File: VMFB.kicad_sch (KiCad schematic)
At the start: 112 parts, among them J1 Barrel_Jack_Switch, J10 Conn_01x03_Pin, J11 Conn_01x06_Pin, J12 Conn_01x04_Pin, J13 Conn_01x04_Pin, J14 Conn_01x04_Pin, J2 USB_B, J3 Screw_Terminal_01x02, J4 Screw_Terminal_01x03, J5 Conn_01x03_Pin, J6 Conn_01x04_Pin, J7 Conn_01x04_Pin, J8 Conn_01x04_Pin, J9 Conn_01x02_Pin, Q1 BC547, Q2 BC547, Q3 BC547, Q4 BD139, Q5 TIP41C, Q6 BC547, U1 LM358, U2 NE555P, U3 NE555P, U4 NE555P, U5 NE555P

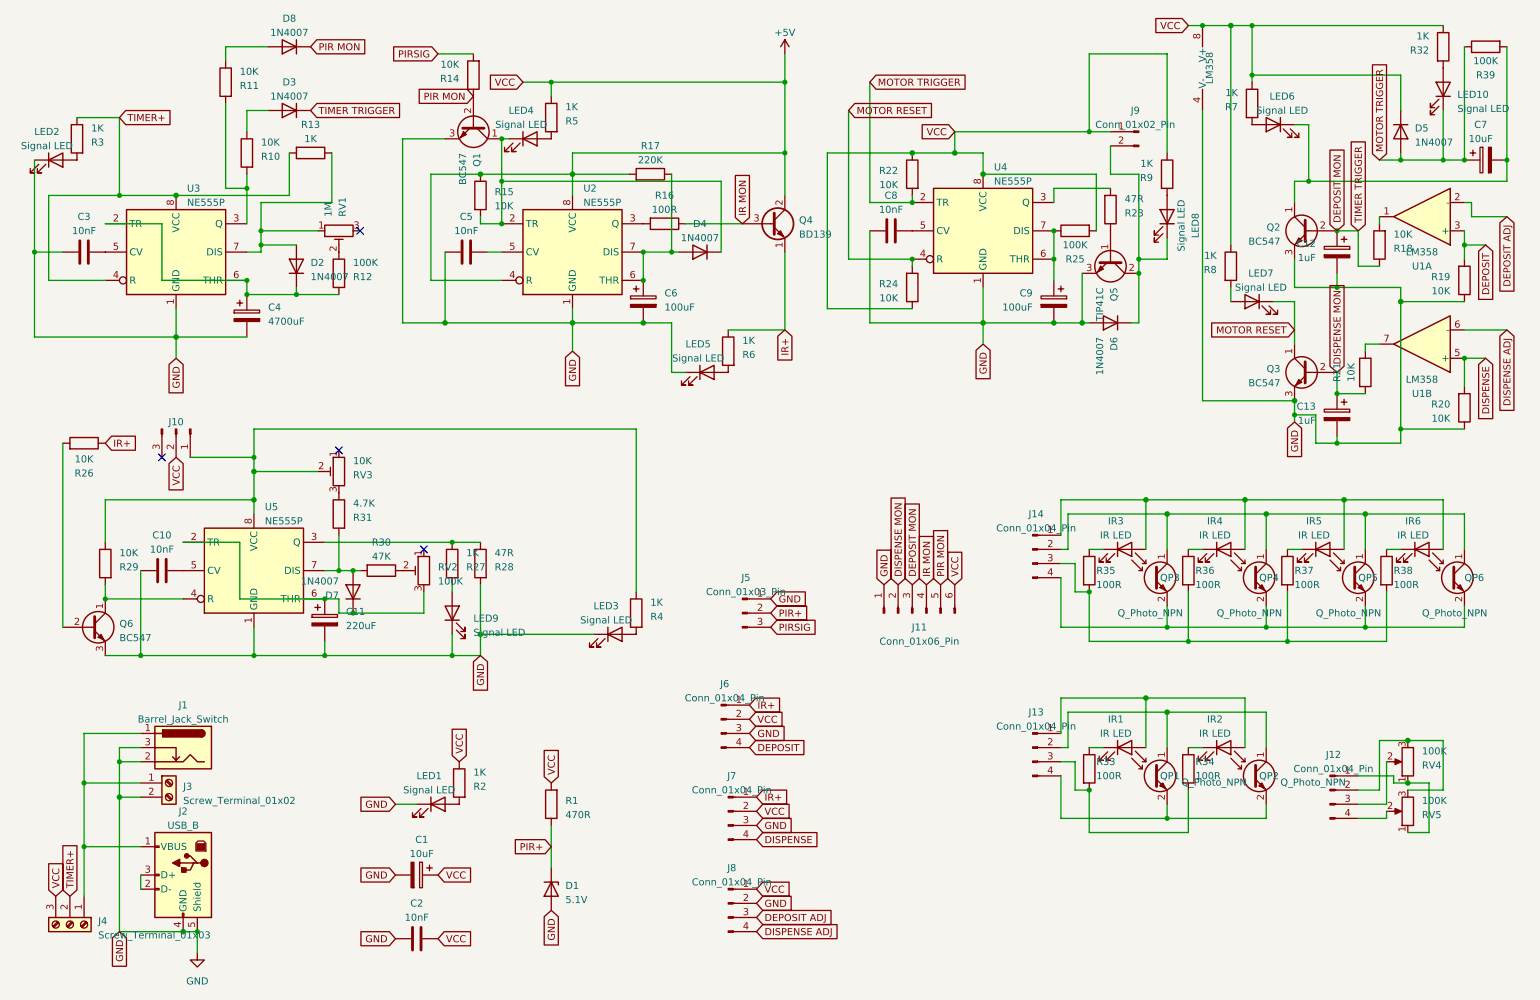
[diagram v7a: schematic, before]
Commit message: changed signal LED resistors to 10K from 1K.
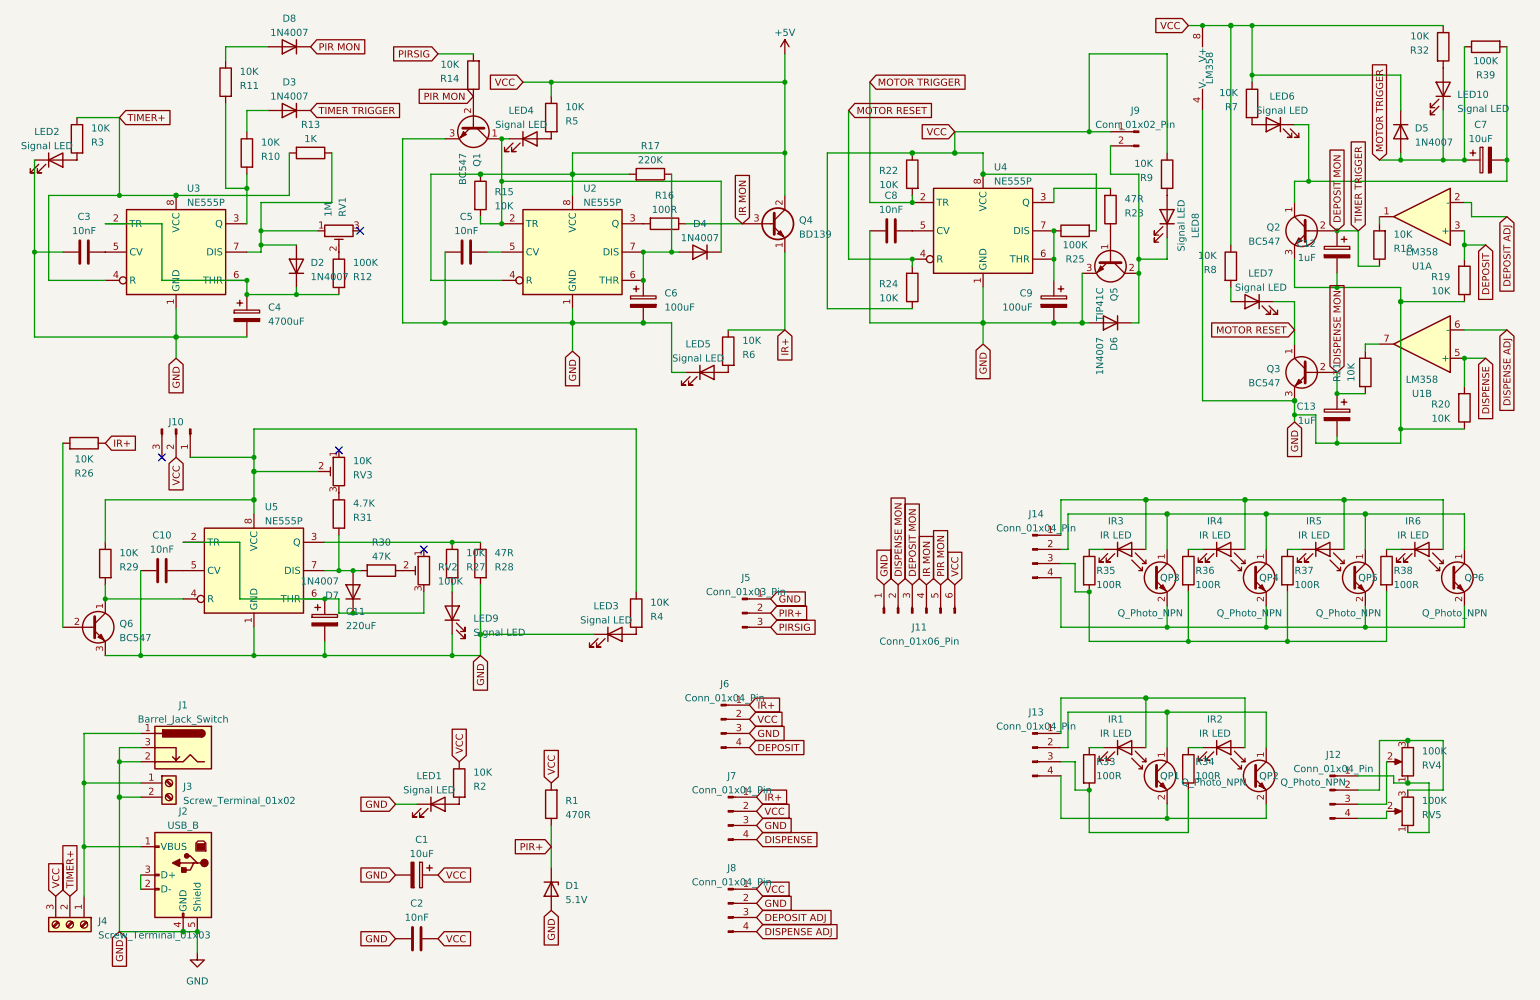
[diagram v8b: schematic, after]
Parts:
- R2, R27, R3, R32, R4, R5, R6, R7, R8, R9: value 1K -> 10K
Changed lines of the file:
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@@
       (effects (font (size 1.27 1.27)) (justify right))
     )
-    (property "Value" "1K" (at 267.97 19.685 0)
+    (property "Value" "10K" (at 267.97 19.685 0)
       (effects (font (size 1.27 1.27)) (justify right))
     )
@@
       (effects (font (size 1.27 1.27)) (justify right))
     )
-    (property "Value" "1K" (at 218.44 42.545 0)
+    (property "Value" "10K" (at 218.44 42.545 0)
       (effects (font (size 1.27 1.27)) (justify right))
     )
@@
       (effects (font (size 1.27 1.27)) (justify right))
     )
-    (property "Value" "1K" (at 144.78 74.295 0)
+    (property "Value" "10K" (at 144.78 74.295 0)
       (effects (font (size 1.27 1.27)) (justify right))
     )
@@
       (effects (font (size 1.27 1.27)) (justify right))
     )
-    (property "Value" "1K" (at 96.52 151.765 0)
+    (property "Value" "10K" (at 96.52 151.765 0)
       (effects (font (size 1.27 1.27)) (justify right))
     )
@@
       (effects (font (size 1.27 1.27)) (justify right))
     )
-    (property "Value" "1K" (at 229.87 59.055 0)
+    (property "Value" "10K" (at 229.87 59.055 0)
       (effects (font (size 1.27 1.27)) (justify right))
     )
@@
       (effects (font (size 1.27 1.27)) (justify right))
     )
-    (property "Value" "1K" (at 95.25 112.395 0)
+    (property "Value" "10K" (at 95.25 112.395 0)
       (effects (font (size 1.27 1.27)) (justify right))
     )
@@
       (effects (font (size 1.27 1.27)) (justify right))
     )
-    (property "Value" "1K" (at 233.68 29.845 0)
+    (property "Value" "10K" (at 233.68 29.845 0)
       (effects (font (size 1.27 1.27)) (justify right))
     )
@@
       (effects (font (size 1.27 1.27)) (justify right))
     )
-    (property "Value" "1K" (at 27.94 36.195 0)
+    (property "Value" "10K" (at 27.94 36.195 0)
       (effects (font (size 1.27 1.27)) (justify right))
     )
@@
       (effects (font (size 1.27 1.27)) (justify right))
     )
-    (property "Value" "1K" (at 128.27 121.285 0)
+    (property "Value" "10K" (at 128.27 121.285 0)
       (effects (font (size 1.27 1.27)) (justify right))
     )
@@
       (effects (font (size 1.27 1.27)) (justify right))
     )
-    (property "Value" "1K" (at 113.03 32.385 0)
-      (effects (font (size 1.27 1.27)) (justify right))
-    )
+    (property "Value" "10K" (at 113.03 32.385 0)
+      (effects (font (size 1.27 1.27)) (justify right))
+    )
